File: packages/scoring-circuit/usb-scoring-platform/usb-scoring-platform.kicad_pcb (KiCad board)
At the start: 4 copper layers, 160 x 100 mm, 187 parts, among them J1 GCT USB4105-GF-A, J10 5520250-2, J12 PD service: GND SDA SCL, J2 STM SWD 3.3V, J3 LEFT WEAPON A B C, J4 RIGHT WEAPON A B C, J5 PISTE - NOT protective earth, J6 ESP 3.3V UART recovery, J7 TST-108-02-G-D - HUB75, J8 645004114822 - panel 5V, J9 5520250-2, Q1 BSS138-7-F, Q2 BSS138-7-F, Q3 BSS138-7-F, Q4 BSS138, Q5 BSS138, SW1 STM RESET, SW2 ESP RESET, SW3 ESP BOOT, U1 STM32G474RET6, U10 SN74AXC1T45DCKR, U11 SN74AXC1T45DCKR, U12 WIZ850io, U13 TSOP38438, U14 SN74AHCT541PWR, U15 SN74AHCT541PWR, U16 4N32M, U17 4N32M, U18 LTM2884IY#PBF, U19 LMR36510ADDAR, U2 ESP32-S3-WROOM-1-N8R8, U20 TPS259470LRPWR, U3 TPD2E2U06DCKR, U4 AP2112K-3.3TRG1, U5 STUSB4500QTR, U6 REC30K-2405SZ, U7 AP63203WU-7, U8 74LVC125APW, U9 74LVC125APW, Y1 ABM3B-8.000MHZ-B2-T

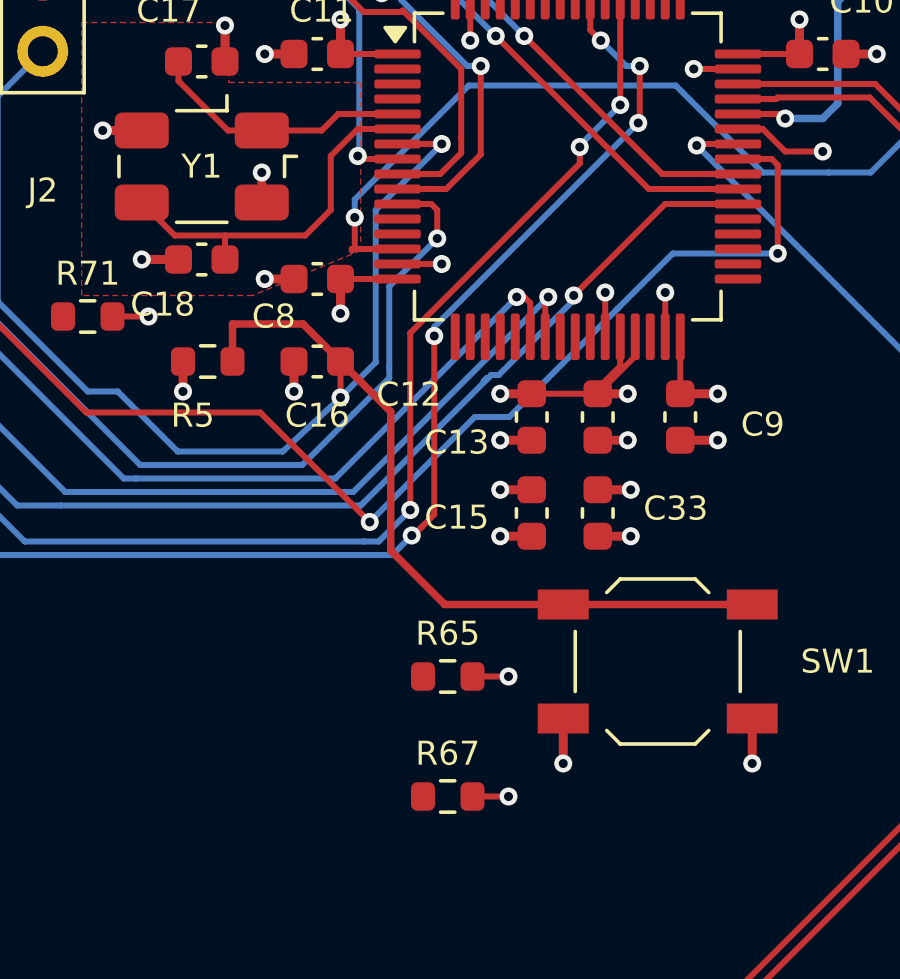
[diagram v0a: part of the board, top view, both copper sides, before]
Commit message: feat(scoring-circuit): route first comparator sense inputs
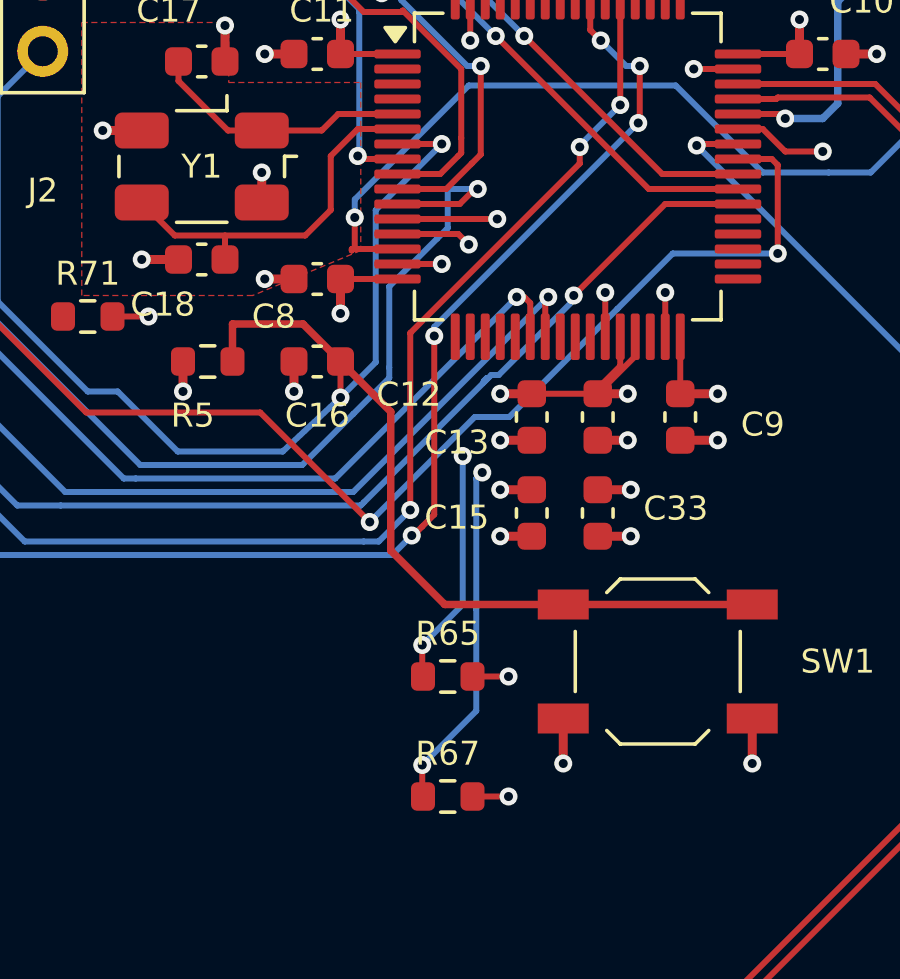
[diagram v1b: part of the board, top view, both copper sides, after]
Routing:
- net LEFT_C_SENSE: track 0.00 -> 23.8 mm, vias 0 -> 3
- net LEFT_A_SENSE: track 0.00 -> 17.6 mm, vias 0 -> 3
- net RIGHT_A_DRIVE: track 61.6 -> 65.0 mm
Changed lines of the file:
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@@
 	)
 	(segment
-		(start 112.45 107.25)
-		(end 112.65 107.45)
+		(start 113.4 107.25)
+		(end 113.9 106.75)
 		(width 0.2)
 		(layer "F.Cu")
@@
 	(segment
 		(start 111.3 107.25)
-		(end 112.45 107.25)
-		(width 0.2)
-		(layer "F.Cu")
-		(net "RIGHT_A_DRIVE")
-	)
-	(segment
-		(start 112.65 107.45)
-		(end 112.65 108.4)
+		(end 113.4 107.25)
+		(width 0.2)
+		(layer "F.Cu")
+		(net "RIGHT_A_DRIVE")
+	)
+	(segment
+		(start 113.9 106.75)
+		(end 114 106.75)
 		(width 0.2)
 		(layer "F.Cu")
@@
 	)
 	(via
-		(at 112.65 108.4)
+		(at 114 106.75)
 		(size 0.6)
 		(drill 0.3)
@@
 	)
 	(segment
+		(start 113 106.75)
+		(end 114 106.75)
+		(width 0.2)
+		(layer "B.Cu")
+		(net "RIGHT_A_DRIVE")
+	)
+	(segment
+		(start 113 108.05)
+		(end 113 106.75)
+		(width 0.2)
+		(layer "B.Cu")
+		(net "RIGHT_A_DRIVE")
+	)
+	(segment
 		(start 111.05 113.05)
 		(end 109.85 114.25)
@@
 	)
 	(segment
+		(start 112.65 108.4)
+		(end 113 108.05)
+		(width 0.2)
+		(layer "B.Cu")
+		(net "RIGHT_A_DRIVE")
+	)
+	(segment
 		(start 111.05 110)
 		(end 111.05 112.7)
@@
 	)
 	(segment
+		(start 111.325 107.75)
+		(end 114.65 107.75)
+		(width 0.2)
+		(layer "F.Cu")
+		(net "LEFT_C_SENSE")
+	)
+	(segment
+		(start 112.15 127)
+		(end 112.175 127)
+		(width 0.2)
+		(layer "F.Cu")
+		(net "LEFT_C_SENSE")
+	)
+	(segment
+		(start 112.15 125.95)
+		(end 112.15 127)
+		(width 0.2)
+		(layer "F.Cu")
+		(net "LEFT_C_SENSE")
+	)
+	(via
+		(at 112.15 125.95)
+		(size 0.6)
+		(drill 0.3)
+		(layers "F.Cu" "B.Cu")
+		(net "LEFT_C_SENSE")
+	)
+	(via
+		(at 114.65 107.75)
+		(size 0.6)
+		(drill 0.3)
+		(layers "F.Cu" "B.Cu")
+		(net "LEFT_C_SENSE")
+	)
+	(via
+		(at 114.15 116.2)
+		(size 0.6)
+		(drill 0.3)
+		(layers "F.Cu" "B.Cu")
+		(net "LEFT_C_SENSE")
+	)
+	(segment
+		(start 114.15 116.2)
+		(end 113.95 116.4)
+		(width 0.2)
+		(layer "B.Cu")
+		(net "LEFT_C_SENSE")
+	)
+	(segment
+		(start 113.95 120.75)
+		(end 113.95 124.15)
+		(width 0.2)
+		(layer "B.Cu")
+		(net "LEFT_C_SENSE")
+	)
+	(segment
+		(start 113.95 116.4)
+		(end 113.95 120.75)
+		(width 0.2)
+		(layer "B.Cu")
+		(net "LEFT_C_SENSE")
+	)
+	(segment
+		(start 113.95 124.15)
+		(end 112.15 125.95)
+		(width 0.2)
+		(layer "B.Cu")
+		(net "LEFT_C_SENSE")
+	)
+	(segment
+		(start 114.65 108.6)
+		(end 113.95 109.3)
+		(width 0.2)
+		(layer "In2.Cu")
+		(net "LEFT_C_SENSE")
+	)
+	(segment
+		(start 114.15 115.45)
+		(end 114.15 116.2)
+		(width 0.2)
+		(layer "In2.Cu")
+		(net "LEFT_C_SENSE")
+	)
+	(segment
+		(start 113.95 109.3)
+		(end 114.1 109.45)
+		(width 0.2)
+		(layer "In2.Cu")
+		(net "LEFT_C_SENSE")
+	)
+	(segment
+		(start 114.1 109.45)
+		(end 114.1 115.4)
+		(width 0.2)
+		(layer "In2.Cu")
+		(net "LEFT_C_SENSE")
+	)
+	(segment
+		(start 114.1 115.4)
+		(end 114.15 115.45)
+		(width 0.2)
+		(layer "In2.Cu")
+		(net "LEFT_C_SENSE")
+	)
+	(segment
+		(start 114.65 107.75)
+		(end 114.65 108.6)
+		(width 0.2)
+		(layer "In2.Cu")
+		(net "LEFT_C_SENSE")
+	)
+	(segment
+		(start 112.15 123)
+		(end 112.175 123)
+		(width 0.2)
+		(layer "F.Cu")
+		(net "LEFT_A_SENSE")
+	)
+	(segment
+		(start 112.15 121.95)
+		(end 112.15 123)
+		(width 0.2)
+		(layer "F.Cu")
+		(net "LEFT_A_SENSE")
+	)
+	(segment
+		(start 113.35 108.25)
+		(end 113.7 108.6)
+		(width 0.2)
+		(layer "F.Cu")
+		(net "LEFT_A_SENSE")
+	)
+	(segment
+		(start 111.325 108.25)
+		(end 113.35 108.25)
+		(width 0.2)
+		(layer "F.Cu")
+		(net "LEFT_A_SENSE")
+	)
+	(via
+		(at 113.7 108.6)
+		(size 0.6)
+		(drill 0.3)
+		(layers "F.Cu" "B.Cu")
+		(net "LEFT_A_SENSE")
+	)
+	(via
+		(at 113.5 115.65)
+		(size 0.6)
+		(drill 0.3)
+		(layers "F.Cu" "B.Cu")
+		(net "LEFT_A_SENSE")
+	)
+	(via
+		(at 112.15 121.95)
+		(size 0.6)
+		(drill 0.3)
+		(layers "F.Cu" "B.Cu")
+		(net "LEFT_A_SENSE")
+	)
+	(segment
+		(start 113.5 120.6)
+		(end 112.15 121.95)
+		(width 0.2)
+		(layer "B.Cu")
+		(net "LEFT_A_SENSE")
+	)
+	(segment
+		(start 113.5 115.65)
+		(end 113.5 120.6)
+		(width 0.2)
+		(layer "B.Cu")
+		(net "LEFT_A_SENSE")
+	)
+	(segment
+		(start 113.5 108.8)
+		(end 113.5 115.65)
+		(width 0.2)
+		(layer "In2.Cu")
+		(net "LEFT_A_SENSE")
+	)
+	(segment
+		(start 113.7 108.6)
+		(end 113.5 108.8)
+		(width 0.2)
+		(layer "In2.Cu")
+		(net "LEFT_A_SENSE")
+	)
+	(segment

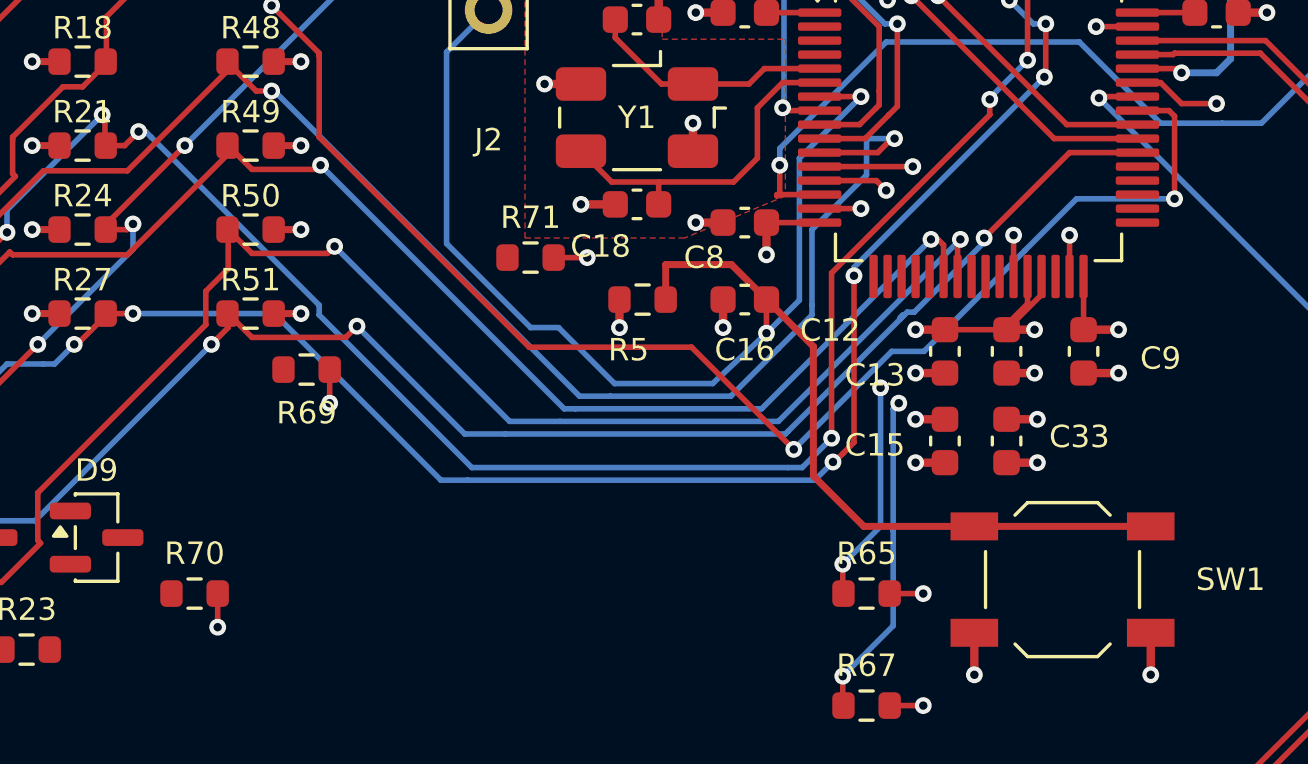
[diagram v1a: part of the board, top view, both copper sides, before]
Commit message: feat(scoring-circuit): route right-side and piste sense inputs
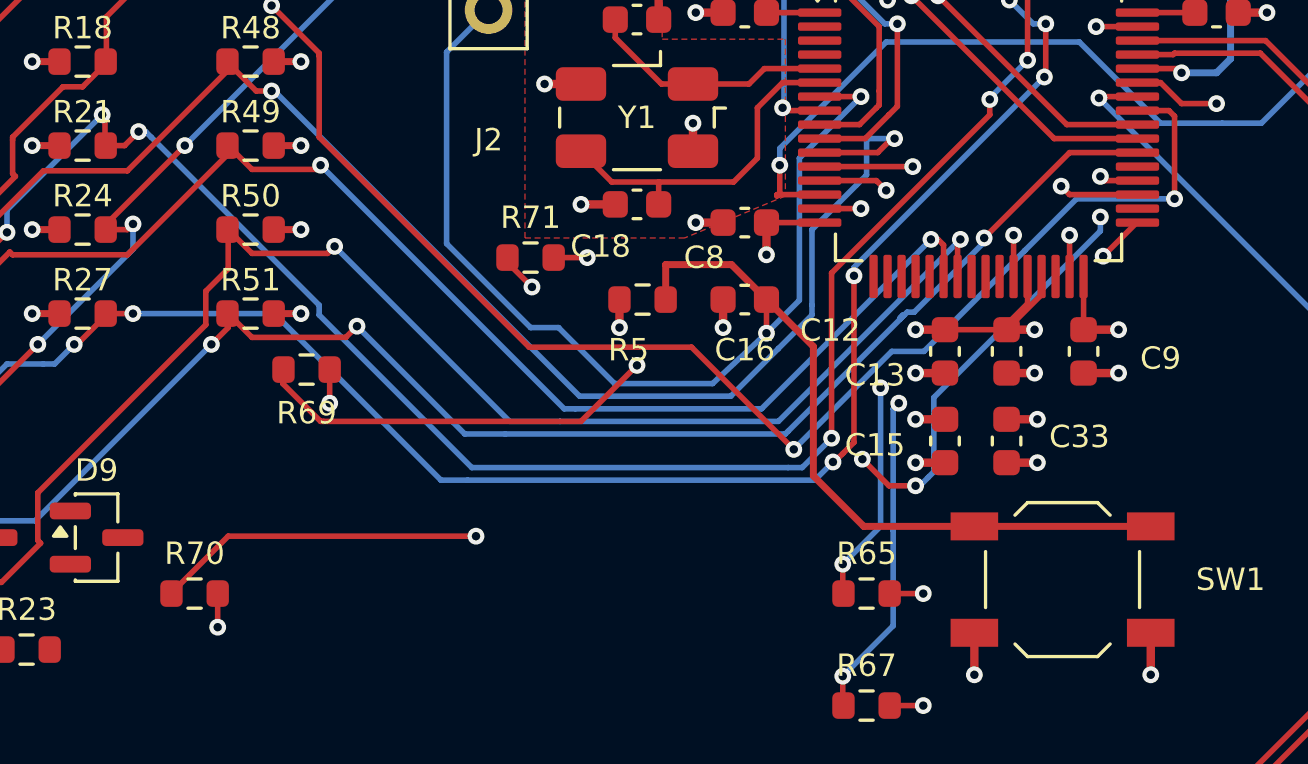
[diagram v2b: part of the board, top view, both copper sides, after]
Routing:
- net RIGHT_C_SENSE: track 0.00 -> 40.6 mm, vias 0 -> 2
- net RIGHT_B_SENSE: track 0.00 -> 38.8 mm, vias 0 -> 2
- net PISTE_SENSE: track 0.00 -> 33.9 mm, vias 0 -> 5

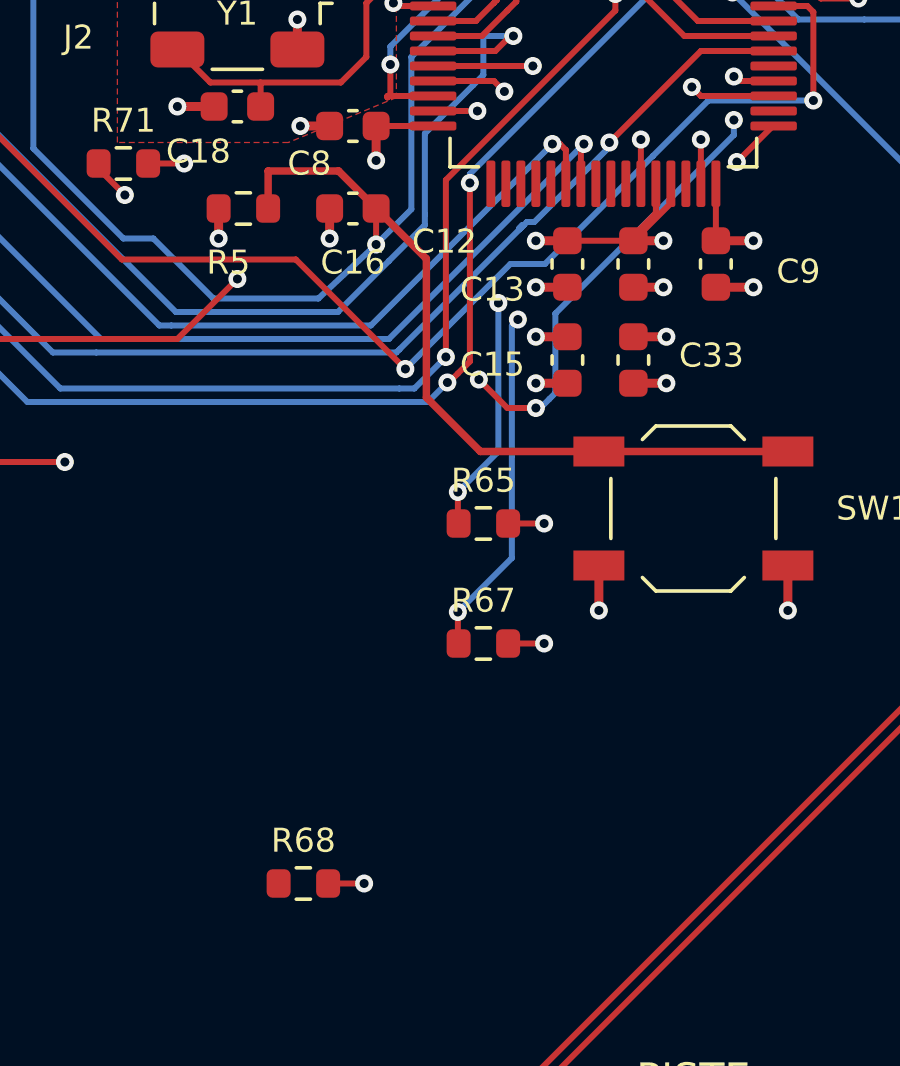
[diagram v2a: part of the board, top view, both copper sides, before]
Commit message: feat(scoring-circuit): open and route right analog sense exit
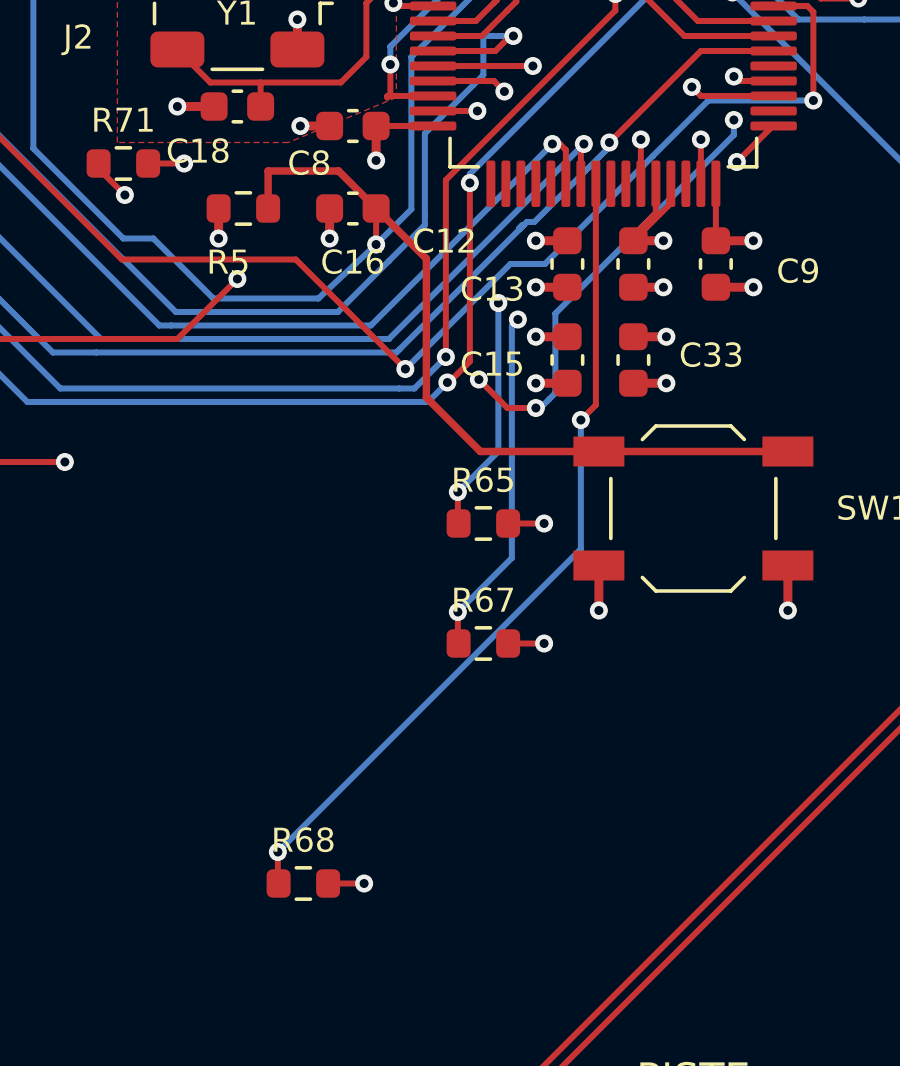
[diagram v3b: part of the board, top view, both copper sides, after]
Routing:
- net RIGHT_A_SENSE: track 0.00 -> 27.8 mm, vias 0 -> 2
- net CORE_3V3: track 185.3 -> 183.2 mm
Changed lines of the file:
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@@
-	)
-	(segment
-		(start 117.825 113.575)
-		(end 115.8 113.575)
-		(width 0.2)
-		(layer "F.Cu")
-		(net "CORE_3V3")
 	)
 	(segment
@@
 	)
 	(segment
+		(start 116.75 119.05)
+		(end 116.25 119.55)
+		(width 0.2)
+		(layer "F.Cu")
+		(net "RIGHT_A_SENSE")
+	)
+	(segment
+		(start 106.15 135)
+		(end 106.175 135)
+		(width 0.2)
+		(layer "F.Cu")
+		(net "RIGHT_A_SENSE")
+	)
+	(segment
+		(start 106.15 133.949999)
+		(end 106.15 135)
+		(width 0.2)
+		(layer "F.Cu")
+		(net "RIGHT_A_SENSE")
+	)
+	(segment
+		(start 116.75 111.65)
+		(end 116.75 119.05)
+		(width 0.2)
+		(layer "F.Cu")
+		(net "RIGHT_A_SENSE")
+	)
+	(segment
+		(start 116.75 111.675)
+		(end 116.75 111.65)
+		(width 0.2)
+		(layer "F.Cu")
+		(net "RIGHT_A_SENSE")
+	)
+	(via
+		(at 106.15 133.949999)
+		(size 0.6)
+		(drill 0.3)
+		(layers "F.Cu" "B.Cu")
+		(net "RIGHT_A_SENSE")
+	)
+	(via
+		(at 116.25 119.55)
+		(size 0.6)
+		(drill 0.3)
+		(layers "F.Cu" "B.Cu")
+		(net "RIGHT_A_SENSE")
+	)
+	(segment
+		(start 116.25 123.85)
+		(end 106.15 133.949999)
+		(width 0.2)
+		(layer "B.Cu")
+		(net "RIGHT_A_SENSE")
+	)
+	(segment
+		(start 116.25 119.55)
+		(end 116.25 123.85)
+		(width 0.2)
+		(layer "B.Cu")
+		(net "RIGHT_A_SENSE")
+	)
+	(segment

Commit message: feat(scoring-circuit): complete comparator input routing
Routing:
- net LEFT_B_SENSE: track 0.00 -> 54.6 mm, vias 0 -> 2
- net RIGHT_B_OE_N: track 75.3 -> 93.3 mm, vias 6 -> 10
- net CORE_3V3: track 183.2 -> 197.4 mm, vias 35 -> 37
